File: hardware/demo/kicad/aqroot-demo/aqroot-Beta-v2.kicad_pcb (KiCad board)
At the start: 6 copper layers, 72 x 148 mm, 311 parts, among them J1 FH69-50S-0.5SH, J2 Molex_5025700893, J3 USB_C_Receptacle_USB2.0_16P, J4 JST-PH-2 BATTERY, J5 COMMUNITY_PORT_1x24, J6 JST-PH-2 SPEAKER, J7 BM02B-ACHSS-GAN-ETF, J8 QWIIC_STEMMA_QT, Q1 AO3400A, Q10 2N7002, Q2 NTMD4820N, Q3 NTMD4820N, Q4 BSS138, Q5 AO3401A, Q6 BSS138, Q7 BSS138, Q8 BSS138, Q9 BSS138, SW1 BOOT, SW2 UP, SW3 DOWN, SW4 LEFT, SW5 RIGHT, SW6 A_SELECT, SW7 B_BACK, SW9 SW_SPDT, U1 ESP32-S3-WROOM-1, U10 USBLC6-2SC6, U11 BQ25185, U12 TPS63020, U13 TPS61023, U14 MAX17048, U16 TCA4307DGKR, U17 TPS61169DCKR, U18 LTC4368-1, U19 TLV7032, U2 PCAL9535APW, U20 TPS22950C, U21 TPS61023, U22 TPS22950C, U3 PCAL9535APW, U4 BMI270, U5 MAX98357A, U6 TSOP38238, U7 E07-400M10S, U8 E22-900M22S, U9 ST25R3916-AQET, Y1 27.12MHz 10pF 3225-4P

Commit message: demo: route USB-C shield tree
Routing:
- net Net-(J3-SHIELD): track 0.00 -> 21.8 mm, vias 0 -> 2
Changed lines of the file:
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@@
+	)
+	(segment
+		(start 47.32 141.625)
+		(end 48.325 141.625)
+		(width 0.3)
+		(layer "F.Cu")
+		(net "Net-(J3-SHIELD)")
+	)
+	(segment
+		(start 50.033265 139.73223)
+		(end 49.125 139.725)
+		(width 0.3)
+		(layer "F.Cu")
+		(net "Net-(J3-SHIELD)")
+	)
+	(via
+		(at 49.125 139.725)
+		(size 0.6)
+		(drill 0.3)
+		(layers "F.Cu" "B.Cu")
+		(net "Net-(J3-SHIELD)")
+	)
+	(via
+		(at 48.325 141.625)
+		(size 0.6)
+		(drill 0.3)
+		(layers "F.Cu" "B.Cu")
+		(net "Net-(J3-SHIELD)")
+	)
+	(segment
+		(start 47.325 143.025)
+		(end 47.325 144.25)
+		(width 0.3)
+		(layer "B.Cu")
+		(net "Net-(J3-SHIELD)")
+	)
+	(segment
+		(start 38.68 145.805)
+		(end 39.65 146.775)
+		(width 0.3)
+		(layer "B.Cu")
+		(net "Net-(J3-SHIELD)")
+	)
+	(segment
+		(start 47.32 145.805)
+		(end 46.35 146.775)
+		(width 0.3)
+		(layer "B.Cu")
+		(net "Net-(J3-SHIELD)")
+	)
+	(segment
+		(start 47.32 141.625)
+		(end 47.325 143.025)
+		(width 0.3)
+		(layer "B.Cu")
+		(net "Net-(J3-SHIELD)")
+	)
+	(segment
+		(start 38.68 145.805)
+		(end 38.675 144.25)
+		(width 0.3)
+		(layer "B.Cu")
+		(net "Net-(J3-SHIELD)")
+	)
+	(segment
+		(start 47.32 145.805)
+		(end 47.325 144.25)
+		(width 0.3)
+		(layer "B.Cu")
+		(net "Net-(J3-SHIELD)")
+	)
+	(segment
+		(start 38.675 144.25)
+		(end 38.675 143.025)
+		(width 0.3)
+		(layer "B.Cu")
+		(net "Net-(J3-SHIELD)")
+	)
+	(segment
+		(start 46.35 146.775)
+		(end 39.65 146.775)
+		(width 0.3)
+		(layer "B.Cu")
+		(net "Net-(J3-SHIELD)")
+	)
+	(segment
+		(start 49.125 139.725)
+		(end 48.325 141.625)
+		(width 0.3)
+		(layer "B.Cu")
+		(net "Net-(J3-SHIELD)")
+	)
+	(segment
+		(start 38.68 141.625)
+		(end 38.675 143.025)
+		(width 0.3)
+		(layer "B.Cu")
+		(net "Net-(J3-SHIELD)")
 	)
 	(segment

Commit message: demo: route LTC4368 fault test branch
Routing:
- net /01_POWER_TREE/LTC4368_FAULT_N: track 88.8 -> 128.6 mm
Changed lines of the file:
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@@
+	)
+	(segment
+		(start 9.775 46.7)
+		(end 8.55 45.5)
+		(width 0.2)
+		(layer "B.Cu")
+		(net "/01_POWER_TREE/LTC4368_FAULT_N")
 	)
 	(segment
@@
 	)
 	(segment
+		(start 8.275 73.05)
+		(end 11.3 71.125)
+		(width 0.2)
+		(layer "B.Cu")
+		(net "/01_POWER_TREE/LTC4368_FAULT_N")
+	)
+	(segment
+		(start 11.3 71.125)
+		(end 11.825 71.125)
+		(width 0.2)
+		(layer "B.Cu")
+		(net "/01_POWER_TREE/LTC4368_FAULT_N")
+	)
+	(segment
 		(start 5.4 29.55)
 		(end 5.65 29)
@@
 	)
 	(segment
+		(start 9.475 48.025)
+		(end 9.775 46.7)
+		(width 0.2)
+		(layer "B.Cu")
+		(net "/01_POWER_TREE/LTC4368_FAULT_N")
+	)
+	(segment
 		(start 5.55 26.1)
 		(end 4.55 24.95)
@@
 	)
 	(segment
+		(start 11.825 71.125)
+		(end 20.5 62.425)
+		(width 0.2)
+		(layer "B.Cu")
+		(net "/01_POWER_TREE/LTC4368_FAULT_N")
+	)
+	(segment
 		(start 7.5 72.95)
 		(end 9.1 72.9)
@@
 	)
 	(segment
+		(start 7.5 73.825)
+		(end 8.275 73.05)
+		(width 0.2)
+		(layer "B.Cu")
+		(net "/01_POWER_TREE/LTC4368_FAULT_N")
+	)
+	(segment
 		(start 4.55 21.15)
 		(end 5.05 19.85)
@@
 	)
 	(segment
+		(start 8.55 45.5)
+		(end 8.5 45.55)
+		(width 0.2)
+		(layer "B.Cu")
+		(net "/01_POWER_TREE/LTC4368_FAULT_N")
+	)
+	(segment
 		(start 5.65 29)
 		(end 5.55 26.1)
@@
 	)
 	(segment
+		(start 8.5 44.5)
+		(end 8.5 45.55)
+		(width 0.2)
+		(layer "B.Cu")
+		(net "/01_POWER_TREE/LTC4368_FAULT_N")
+	)
+	(segment
 		(start 4.8 67.2)
 		(end 4.8 69.1)
@@
 		(layer "B.Cu")
 		(net "/01_POWER_TREE/LTC4368_FAULT_N")
+	)
+	(segment
+		(start 20.5 62.425)
+		(end 9.475 48.025)
+		(width 0.2)
+		(layer "B.Cu")
+		(net "/01_POWER_TREE/LTC4368_FAULT_N")

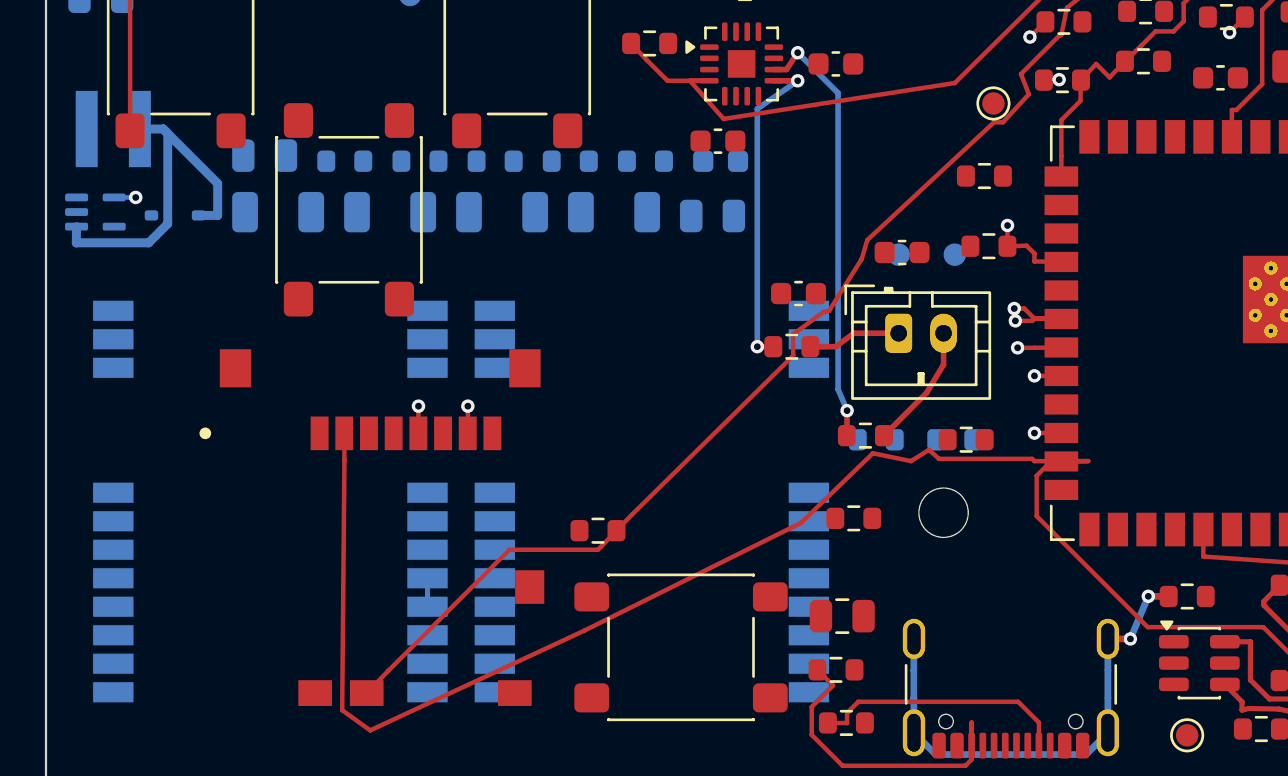
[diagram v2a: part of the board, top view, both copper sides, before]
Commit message: demo: route LoRa busy control
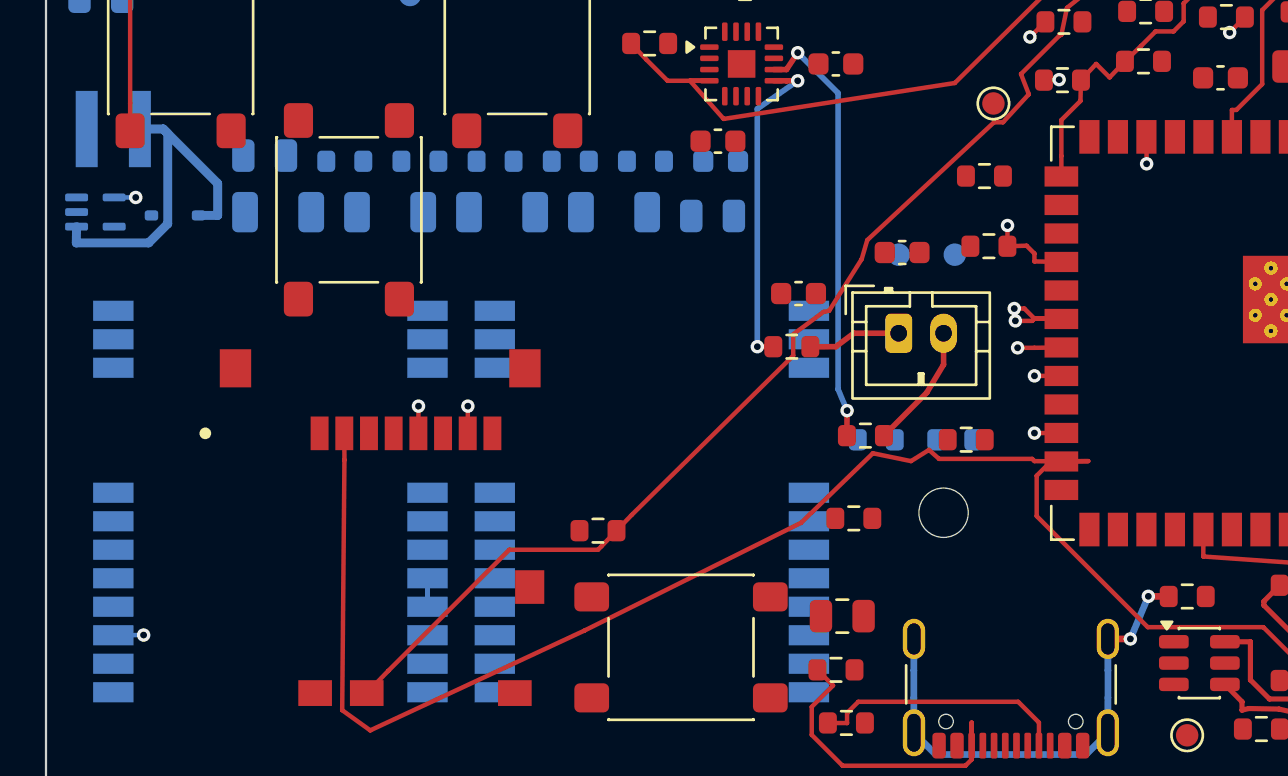
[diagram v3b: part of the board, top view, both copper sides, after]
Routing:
- net /SX1262_BUSY: track 0.00 -> 58.7 mm, vias 0 -> 2
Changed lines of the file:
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@@
+	)
+	(segment
+		(start 49.04 119.25)
+		(end 49.05 120.45)
+		(width 0.2)
+		(layer "F.Cu")
+		(net "/SX1262_BUSY")
+	)
+	(via
+		(at 49.05 120.45)
+		(size 0.6)
+		(drill 0.3)
+		(layers "F.Cu" "B.Cu")
+		(net "/SX1262_BUSY")
+	)
+	(via
+		(at 4.35 141.45)
+		(size 0.6)
+		(drill 0.3)
+		(layers "F.Cu" "B.Cu")
+		(net "/SX1262_BUSY")
+	)
+	(segment
+		(start 3 141.46)
+		(end 4.35 141.45)
+		(width 0.2)
+		(layer "B.Cu")
+		(net "/SX1262_BUSY")
+	)
+	(segment
+		(start 49.05 120.45)
+		(end 44.95 132.55)
+		(width 0.2)
+		(layer "In2.Cu")
+		(net "/SX1262_BUSY")
+	)
+	(segment
+		(start 44.95 132.55)
+		(end 43.55 133.8)
+		(width 0.2)
+		(layer "In2.Cu")
+		(net "/SX1262_BUSY")
+	)
+	(segment
+		(start 43.55 133.8)
+		(end 40.3 131.25)
+		(width 0.2)
+		(layer "In2.Cu")
+		(net "/SX1262_BUSY")
+	)
+	(segment
+		(start 40.3 131.25)
+		(end 4.35 141.45)
+		(width 0.2)
+		(layer "In2.Cu")
+		(net "/SX1262_BUSY")
 	)
 	(segment

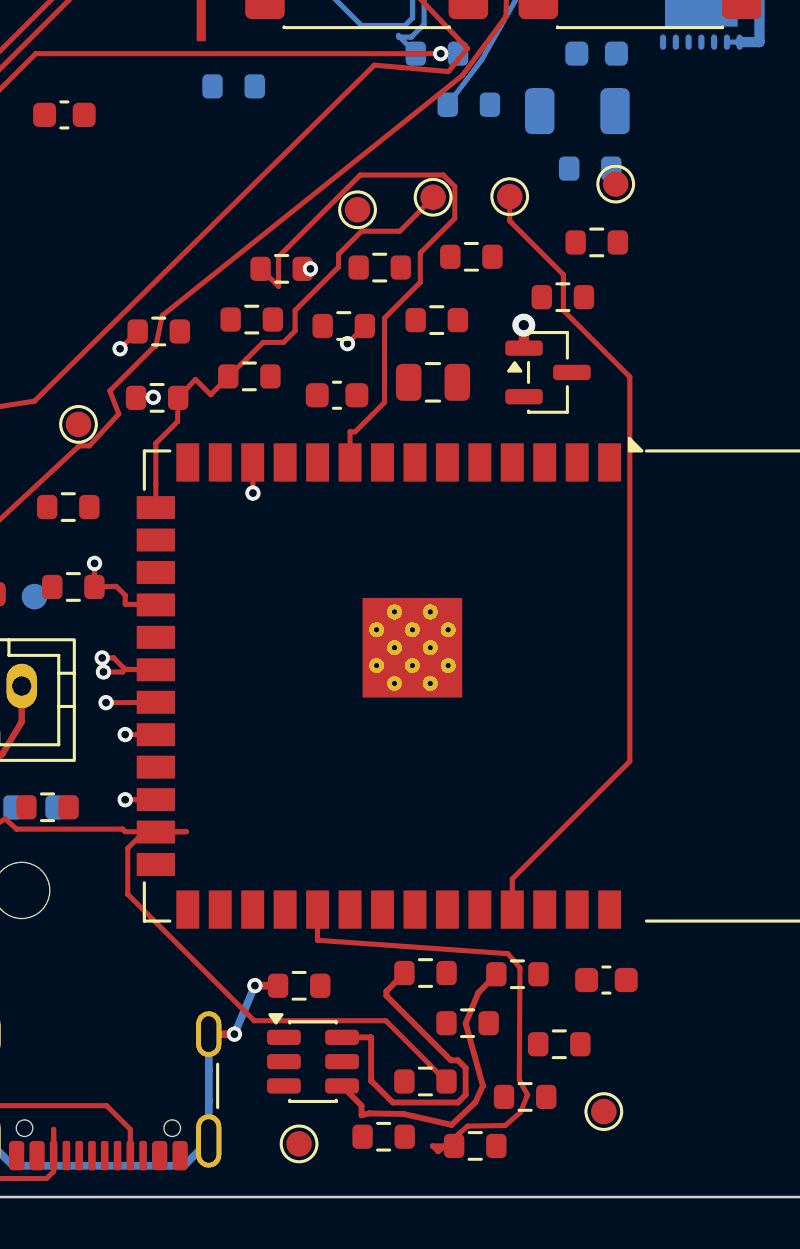
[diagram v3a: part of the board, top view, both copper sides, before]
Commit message: demo: route GPIO45 VDD SPI strap
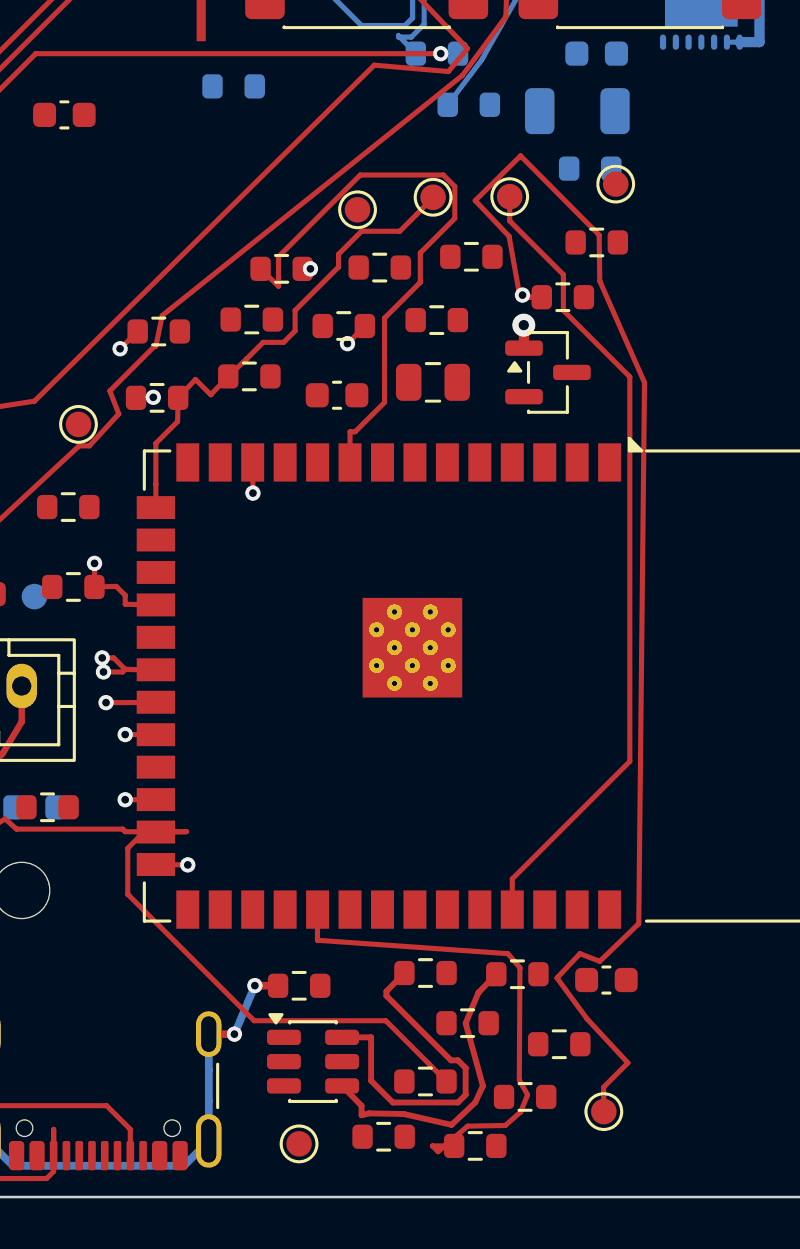
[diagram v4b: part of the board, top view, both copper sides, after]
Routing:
- net /02_MCU_CORE/GPIO45_VDDSPI_STRAP: track 0.00 -> 79.8 mm, vias 0 -> 2
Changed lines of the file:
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@@
+	)
+	(segment
+		(start 64.375 116.125)
+		(end 64.15 137.3)
+		(width 0.2)
+		(layer "F.Cu")
+		(net "/02_MCU_CORE/GPIO45_VDDSPI_STRAP")
+	)
+	(segment
+		(start 60.95 139.425)
+		(end 62.125 141.025)
+		(width 0.2)
+		(layer "F.Cu")
+		(net "/02_MCU_CORE/GPIO45_VDDSPI_STRAP")
+	)
+	(segment
+		(start 59.55 112.7)
+		(end 59.6 112.7)
+		(width 0.2)
+		(layer "F.Cu")
+		(net "/02_MCU_CORE/GPIO45_VDDSPI_STRAP")
+	)
+	(segment
+		(start 61.85 138.475)
+		(end 60.95 139.425)
+		(width 0.2)
+		(layer "F.Cu")
+		(net "/02_MCU_CORE/GPIO45_VDDSPI_STRAP")
+	)
+	(segment
+		(start 60.354437 112.781624)
+		(end 59.45 112.8)
+		(width 0.2)
+		(layer "F.Cu")
+		(net "/02_MCU_CORE/GPIO45_VDDSPI_STRAP")
+	)
+	(segment
+		(start 59.525 107.25)
+		(end 62.6 110.35)
+		(width 0.2)
+		(layer "F.Cu")
+		(net "/02_MCU_CORE/GPIO45_VDDSPI_STRAP")
+	)
+	(segment
+		(start 59.45 112.8)
+		(end 59.55 112.7)
+		(width 0.2)
+		(layer "F.Cu")
+		(net "/02_MCU_CORE/GPIO45_VDDSPI_STRAP")
+	)
+	(segment
+		(start 57.75 109)
+		(end 59.525 107.25)
+		(width 0.2)
+		(layer "F.Cu")
+		(net "/02_MCU_CORE/GPIO45_VDDSPI_STRAP")
+	)
+	(segment
+		(start 62.782986 144.656201)
+		(end 62.775 143.7)
+		(width 0.2)
+		(layer "F.Cu")
+		(net "/02_MCU_CORE/GPIO45_VDDSPI_STRAP")
+	)
+	(segment
+		(start 64.15 137.3)
+		(end 62.625 138.775)
+		(width 0.2)
+		(layer "F.Cu")
+		(net "/02_MCU_CORE/GPIO45_VDDSPI_STRAP")
+	)
+	(segment
+		(start 62.625 138.775)
+		(end 61.85 138.475)
+		(width 0.2)
+		(layer "F.Cu")
+		(net "/02_MCU_CORE/GPIO45_VDDSPI_STRAP")
+	)
+	(segment
+		(start 59.5 112.775)
+		(end 59.075 110.4)
+		(width 0.2)
+		(layer "F.Cu")
+		(net "/02_MCU_CORE/GPIO45_VDDSPI_STRAP")
+	)
+	(segment
+		(start 45.25 134.985)
+		(end 46.5 135)
+		(width 0.2)
+		(layer "F.Cu")
+		(net "/02_MCU_CORE/GPIO45_VDDSPI_STRAP")
+	)
+	(segment
+		(start 63.725 142.75)
+		(end 62.775 143.7)
+		(width 0.2)
+		(layer "F.Cu")
+		(net "/02_MCU_CORE/GPIO45_VDDSPI_STRAP")
+	)
+	(segment
+		(start 59.075 110.4)
+		(end 57.75 109)
+		(width 0.2)
+		(layer "F.Cu")
+		(net "/02_MCU_CORE/GPIO45_VDDSPI_STRAP")
+	)
+	(segment
+		(start 62.125 141.025)
+		(end 63.725 142.75)
+		(width 0.2)
+		(layer "F.Cu")
+		(net "/02_MCU_CORE/GPIO45_VDDSPI_STRAP")
+	)
+	(segment
+		(start 62.625 112.15)
+		(end 64.375 116.125)
+		(width 0.2)
+		(layer "F.Cu")
+		(net "/02_MCU_CORE/GPIO45_VDDSPI_STRAP")
+	)
+	(segment
+		(start 60.354437 112.781624)
+		(end 59.5 112.775)
+		(width 0.2)
+		(layer "F.Cu")
+		(net "/02_MCU_CORE/GPIO45_VDDSPI_STRAP")
+	)
+	(segment
+		(start 62.6 110.35)
+		(end 62.625 112.15)
+		(width 0.2)
+		(layer "F.Cu")
+		(net "/02_MCU_CORE/GPIO45_VDDSPI_STRAP")
+	)
+	(via
+		(at 46.5 135)
+		(size 0.6)
+		(drill 0.3)
+		(layers "F.Cu" "B.Cu")
+		(net "/02_MCU_CORE/GPIO45_VDDSPI_STRAP")
+	)
+	(via
+		(at 59.6 112.7)
+		(size 0.6)
+		(drill 0.3)
+		(layers "F.Cu" "B.Cu")
+		(net "/02_MCU_CORE/GPIO45_VDDSPI_STRAP")
+	)
+	(segment
+		(start 46.5 135)
+		(end 60.175 115.8)
+		(width 0.2)
+		(layer "In2.Cu")
+		(net "/02_MCU_CORE/GPIO45_VDDSPI_STRAP")
+	)
+	(segment
+		(start 60.175 115.8)
+		(end 60.55 113.575)
+		(width 0.2)
+		(layer "In2.Cu")
+		(net "/02_MCU_CORE/GPIO45_VDDSPI_STRAP")
+	)
+	(segment
+		(start 59.625 112.675)
+		(end 59.6 112.7)
+		(width 0.2)
+		(layer "In2.Cu")
+		(net "/02_MCU_CORE/GPIO45_VDDSPI_STRAP")
+	)
+	(segment
+		(start 60.55 113.575)
+		(end 59.625 112.675)
+		(width 0.2)
+		(layer "In2.Cu")
+		(net "/02_MCU_CORE/GPIO45_VDDSPI_STRAP")
 	)
 	(segment

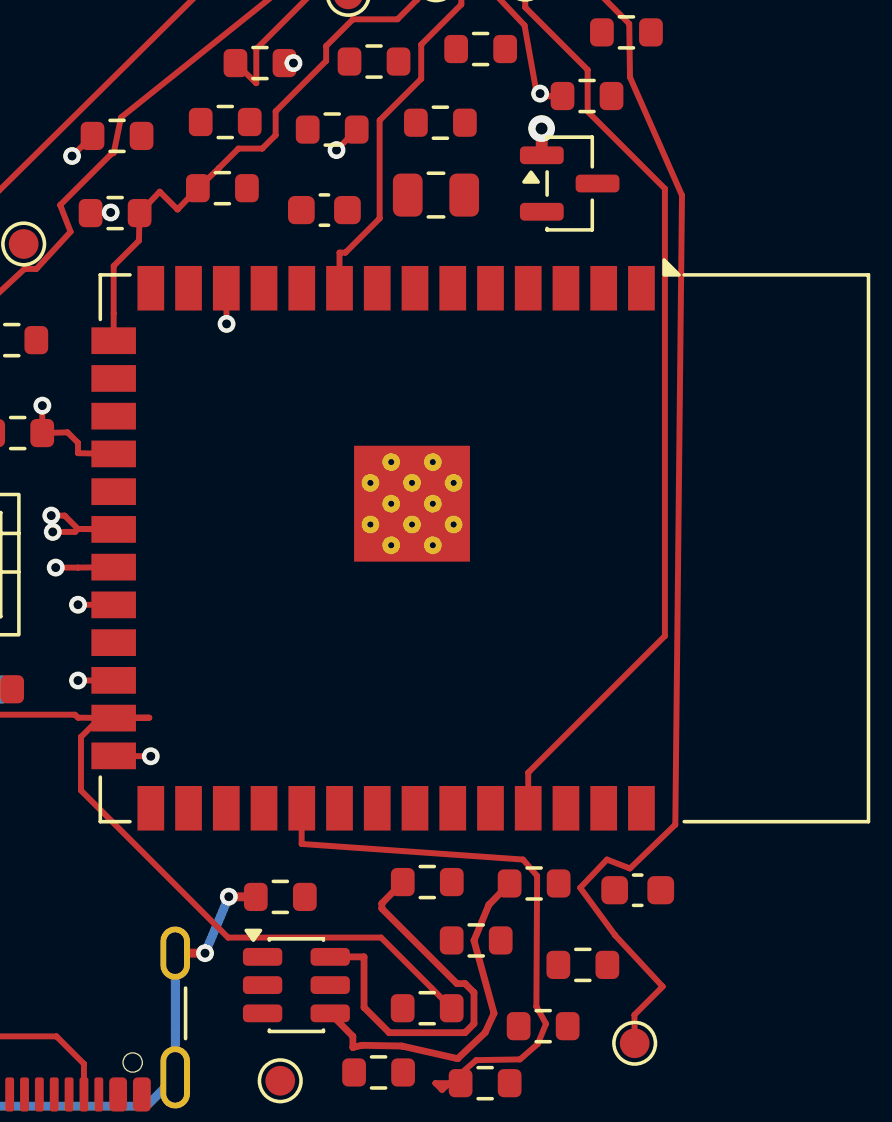
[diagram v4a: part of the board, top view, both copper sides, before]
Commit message: demo: route ESP32 enable reset tree
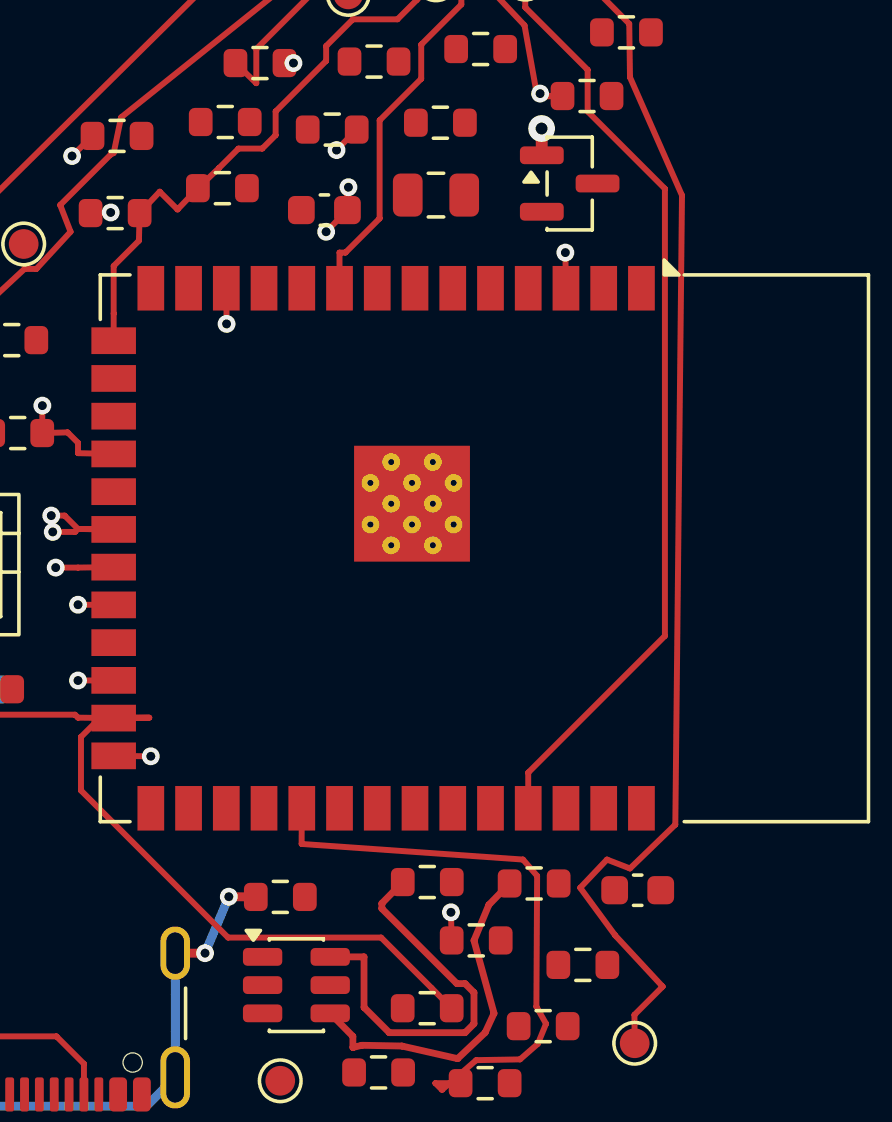
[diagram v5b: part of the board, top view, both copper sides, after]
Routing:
- net Net-(U1-EN): track 0.00 -> 46.0 mm, vias 0 -> 4
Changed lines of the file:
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@@
+	)
+	(segment
+		(start 53.15 115.75)
+		(end 53.15 115.85)
+		(width 0.2)
+		(layer "F.Cu")
+		(net "Net-(U1-EN)")
+	)
+	(segment
+		(start 53.116474 116.619848)
+		(end 52.4 117.35)
+		(width 0.2)
+		(layer "F.Cu")
+		(net "Net-(U1-EN)")
+	)
+	(segment
+		(start 53.1 115.7)
+		(end 53.15 115.75)
+		(width 0.2)
+		(layer "F.Cu")
+		(net "Net-(U1-EN)")
+	)
+	(segment
+		(start 53.116474 116.619848)
+		(end 53.1 115.7)
+		(width 0.2)
+		(layer "F.Cu")
+		(net "Net-(U1-EN)")
+	)
+	(segment
+		(start 56.624525 141.196579)
+		(end 56.6 140.25)
+		(width 0.2)
+		(layer "F.Cu")
+		(net "Net-(U1-EN)")
+	)
+	(segment
+		(start 60.47 119.25)
+		(end 60.45 118.05)
+		(width 0.2)
+		(layer "F.Cu")
+		(net "Net-(U1-EN)")
+	)
+	(via
+		(at 60.45 118.05)
+		(size 0.6)
+		(drill 0.3)
+		(layers "F.Cu" "B.Cu")
+		(net "Net-(U1-EN)")
+	)
+	(via
+		(at 52.4 117.35)
+		(size 0.6)
+		(drill 0.3)
+		(layers "F.Cu" "B.Cu")
+		(net "Net-(U1-EN)")
+	)
+	(via
+		(at 53.15 115.85)
+		(size 0.6)
+		(drill 0.3)
+		(layers "F.Cu" "B.Cu")
+		(net "Net-(U1-EN)")
+	)
+	(via
+		(at 56.6 140.25)
+		(size 0.6)
+		(drill 0.3)
+		(layers "F.Cu" "B.Cu")
+		(net "Net-(U1-EN)")
+	)
+	(segment
+		(start 45.95 135.35)
+		(end 54.275 142.575)
+		(width 0.2)
+		(layer "In2.Cu")
+		(net "Net-(U1-EN)")
+	)
+	(segment
+		(start 54.275 142.575)
+		(end 56.6 140.25)
+		(width 0.2)
+		(layer "In2.Cu")
+		(net "Net-(U1-EN)")
+	)
+	(segment
+		(start 52.4 117.35)
+		(end 45.1 133.25)
+		(width 0.2)
+		(layer "In2.Cu")
+		(net "Net-(U1-EN)")
+	)
+	(segment
+		(start 45.1 133.25)
+		(end 45.95 135.35)
+		(width 0.2)
+		(layer "In2.Cu")
+		(net "Net-(U1-EN)")
+	)
+	(segment
+		(start 60.45 118.05)
+		(end 53.15 115.85)
+		(width 0.2)
+		(layer "In3.Cu")
+		(net "Net-(U1-EN)")
 	)
 	(segment
